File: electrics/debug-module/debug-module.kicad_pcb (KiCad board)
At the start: 2 copper layers, 40.6 x 30.4 mm, 25 parts, among them J1 East, J2 West, J3 USB_B_Micro, U1 FT231XS, U2 LD1117S33

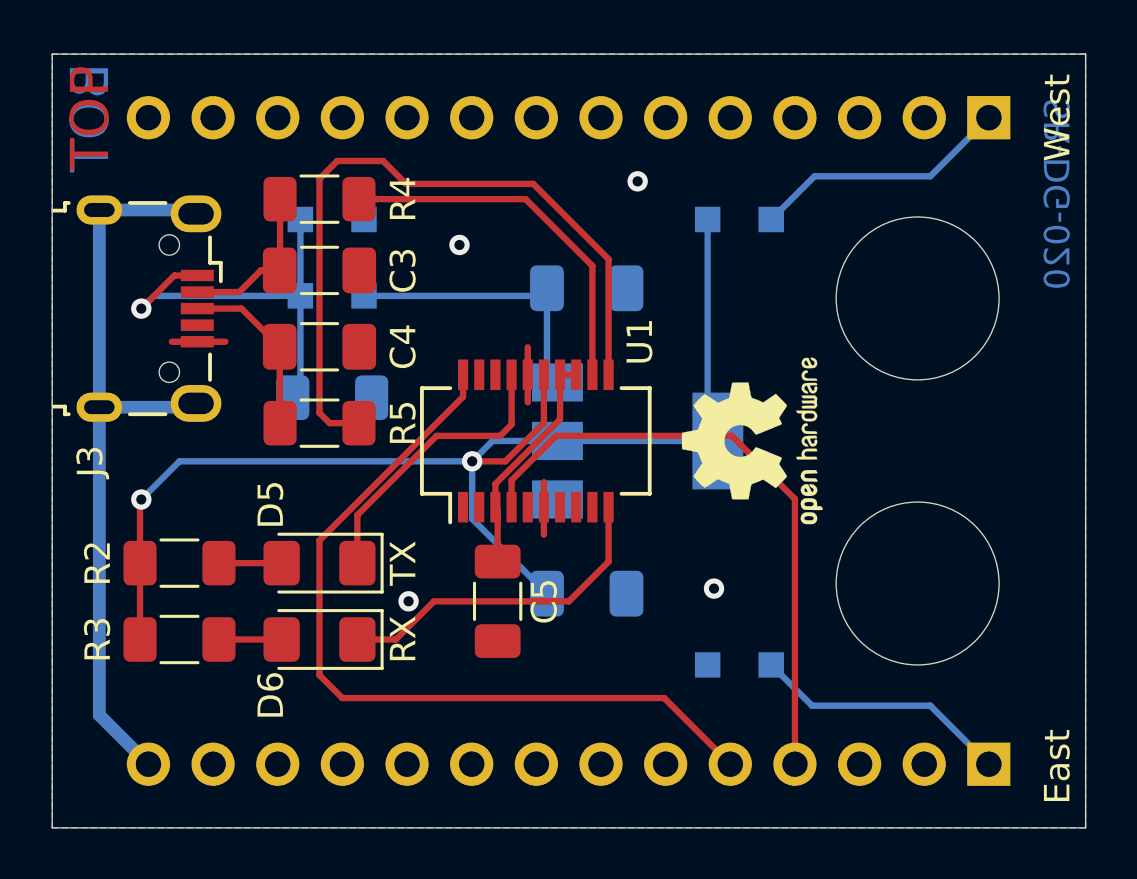
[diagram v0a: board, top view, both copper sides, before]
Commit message: Fix all ERC and DRC warnings during build
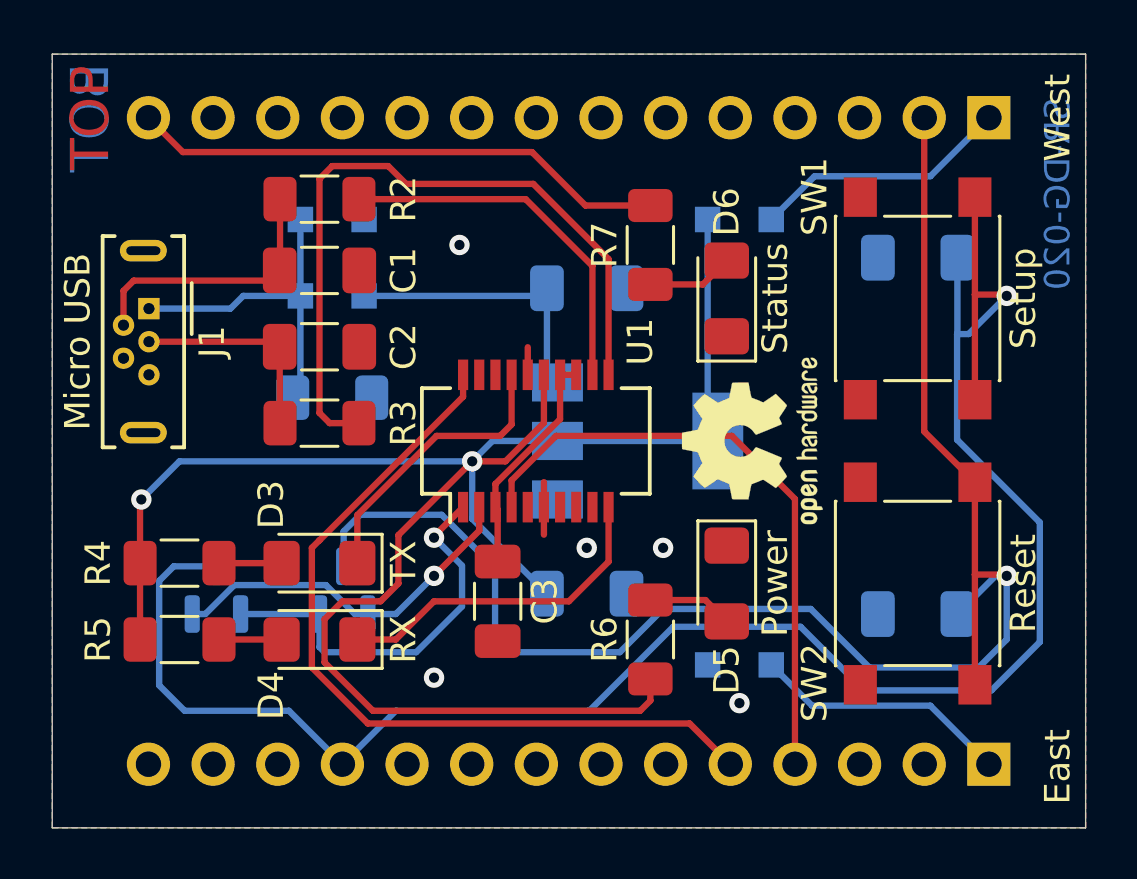
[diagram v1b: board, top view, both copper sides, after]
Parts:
- removed the G1 at (156.0, 103.0)
- removed H1: Reset, MountingHole:MountingHole_6.4mm_M6
- removed H2: Status, MountingHole:MountingHole_6.4mm_M6
- added C6: 1nF, Capacitor_SMD:C_1206_3216Metric_Pad1.33x1.80mm_HandSolder, B.Cu at (154.0, 88.0)
- added C7: 1nF, Capacitor_SMD:C_1206_3216Metric_Pad1.33x1.80mm_HandSolder, B.Cu at (154.0, 102.0)
- added D5: Power, LED_SMD:LED_1206_3216Metric_Pad1.42x1.75mm_HandSolder, F.Cu at (146.5, 100.8)
- added D6: Status, LED_SMD:LED_1206_3216Metric_Pad1.42x1.75mm_HandSolder, F.Cu at (146.5, 89.6)
- added Q1: S8050, Package_TO_SOT_SMD:SOT-23, B.Cu at (131.4, 101.1)
- added Q2: S8050, Package_TO_SOT_SMD:SOT-23, B.Cu at (126.5, 101.1)
- added R5: 220R, Resistor_SMD:R_1206_3216Metric_Pad1.30x1.75mm_HandSolder, F.Cu at (125.0, 103.0)
- added R7: 220R, Resistor_SMD:R_1206_3216Metric_Pad1.30x1.75mm_HandSolder, F.Cu at (143.5, 87.5)
- added SW1: Setup, Button_Switch_SMD:SW_SPST_PTS645, F.Cu at (154.0, 89.6)
- added SW2: Reset, Button_Switch_SMD:SW_SPST_PTS645, F.Cu at (154.0, 100.8)
- J1: renamed from J3; value USB_B_Micro -> Micro USB; footprint Connector_USB:USB_Micro-B_Wuerth_629105150521 -> Connector_USB:USB_Micro-B_Wuerth_614105150721_Vertical
- moved R6 18.5 mm to (143.5, 103.0), turned to 90 degrees
- renumbered C3 to C1, C4 to C2, C5 to C3, C1 to C4, C2 to C5, D5 to D3, D6 to D4, D3 to D7, D4 to D8, G2 to G1, J1 to J2, J2 to J3, R4 to R2, R5 to R3, R2 to R4, R3 to R6
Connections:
- D4 pad 2: Net-(D6-Pad2) -> Net-(D4-Pad2)
- J1 pad 4: (no net) -> unconnected-(J1-Pad4)
- J1 pad 6: GNDPWR -> GND
- J2 pad 10: (no net) -> unconnected-(J2-Pad10)
- J2 pad 11: (no net) -> Panel_Setup
- J2 pad 12: (no net) -> unconnected-(J2-Pad12)
- J2 pad 13: (no net) -> unconnected-(J2-Pad13)
- J2 pad 14: GNDPWR -> GND
- J2 pad 2: (no net) -> unconnected-(J2-Pad2)
- J2 pad 3: (no net) -> unconnected-(J2-Pad3)
- J2 pad 6: (no net) -> unconnected-(J2-Pad6)
- J2 pad 7: (no net) -> unconnected-(J2-Pad7)
- J2 pad 8: (no net) -> unconnected-(J2-Pad8)
- J2 pad 9: (no net) -> unconnected-(J2-Pad9)
- J3 pad 10: (no net) -> unconnected-(J3-Pad10)
- J3 pad 11: (no net) -> unconnected-(J3-Pad11)
- J3 pad 12: (no net) -> unconnected-(J3-Pad12)
- J3 pad 13: (no net) -> unconnected-(J3-Pad13)
- J3 pad 14: (no net) -> Panel_Status
- J3 pad 2: (no net) -> Panel_Reset
- J3 pad 3: (no net) -> unconnected-(J3-Pad3)
- J3 pad 4: (no net) -> unconnected-(J3-Pad4)
- J3 pad 5: (no net) -> unconnected-(J3-Pad5)
- J3 pad 6: (no net) -> unconnected-(J3-Pad6)
- J3 pad 7: (no net) -> unconnected-(J3-Pad7)
- J3 pad 8: (no net) -> unconnected-(J3-Pad8)
- J3 pad 9: (no net) -> unconnected-(J3-Pad9)
- R6 pad 2: Net-(D6-Pad2) -> Net-(D5-Pad2)
- U1 pad 1: (no net) -> FT_~{DTR}
- U1 pad 18: (no net) -> unconnected-(U1-Pad18)
- U1 pad 19: (no net) -> unconnected-(U1-Pad19)
- U1 pad 2: (no net) -> FT_~{RTS}
- U1 pad 5: (no net) -> unconnected-(U1-Pad5)
- U1 pad 7: (no net) -> unconnected-(U1-Pad7)
- U1 pad 8: (no net) -> unconnected-(U1-Pad8)
- U1 pad 9: (no net) -> unconnected-(U1-Pad9)
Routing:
- net Panel_Setup: track 0.00 -> 74.8 mm, vias 0 -> 1
- net Panel_Reset: track 0.00 -> 63.0 mm, vias 0 -> 1
- net GNDPWR: track 30.3 -> 0.00 mm
- net +3V3: track 49.7 -> 75.5 mm
- net Panel_Status: track 0.00 -> 21.1 mm
- net FT_~{DTR}: track 0.00 -> 15.7 mm, vias 0 -> 1
- net FT_~{RTS}: track 0.00 -> 14.5 mm, vias 0 -> 1
- net USB_DM: track 6.39 -> 10.6 mm
- net Net-(D5-Pad2): track 0.00 -> 3.35 mm
- net GND: track 6.33 -> 3.15 mm, vias 4 -> 5
- net Net-(D1-Pad1): track 16.3 -> 13.3 mm, vias 1 -> 0
- net Net-(D4-Pad2): track 0.00 -> 2.46 mm
- net USB_DP: track 6.86 -> 8.23 mm
- net Net-(D6-Pad2): track 2.46 -> 3.39 mm
- net (no net): track 0.51 -> 0.00 mm
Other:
- board text added: "GrayC GmbH https://docs.inoa.io"
- board text removed: "Inoa Satellite v2.0 GrayC GmbH https://docs.inoa.io"
